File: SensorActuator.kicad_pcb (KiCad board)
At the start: 2 copper layers, 32 parts, among them IC1 STM32L051K8T6, P1 CONN_02X06, P3 CONN_02X04, P4 CONN_01X04, P5 CONN_01X02, Q1 PMosfetGen, Q2 PMosfetGen, Q4 PMosfetGen, Q5 AO3401, SW1 SW_PUSH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

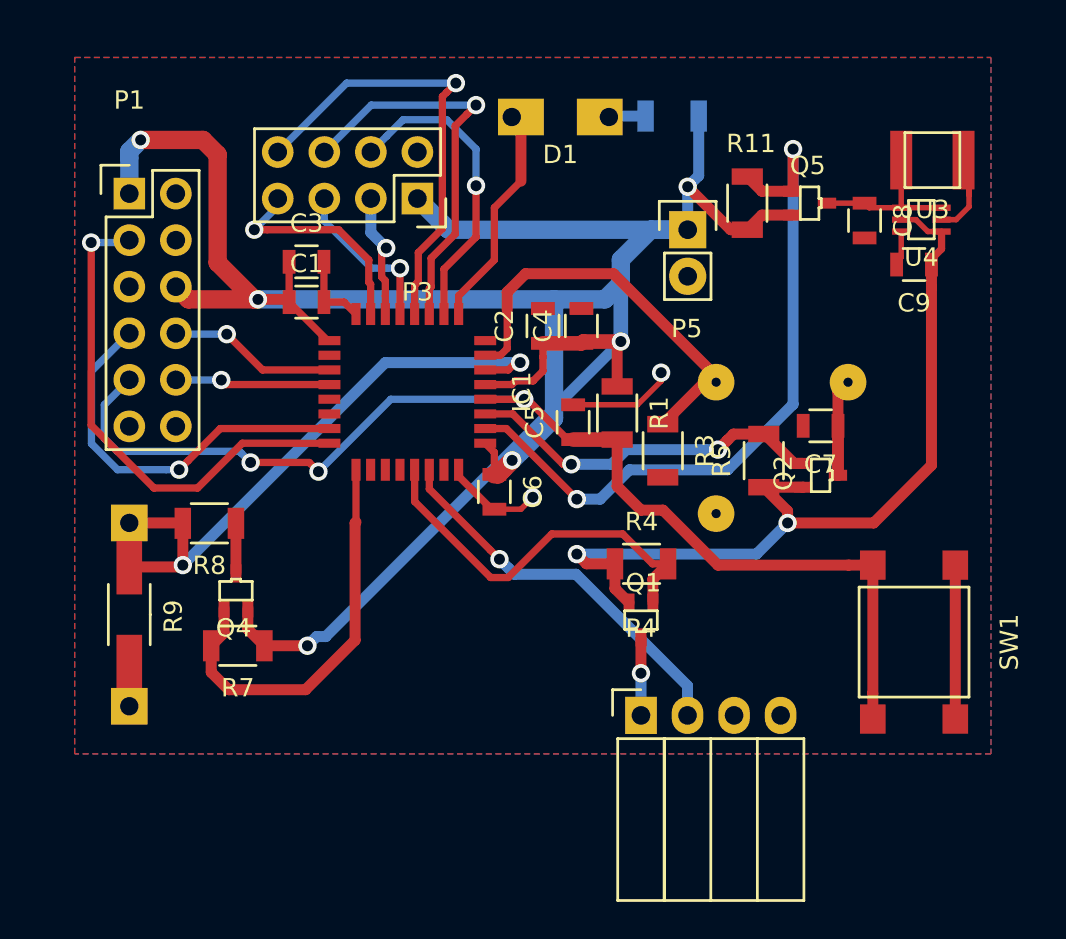
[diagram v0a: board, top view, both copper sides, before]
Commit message: Version 2 of the pcb
 * PCB is now exact 50x38 mm, so we can print it on a small board
 * Through hole components have only a pad on one side,
     this way we are sure we connect the correct pad

Signed-off-by: Philip Luyckx <philip.luyckx@gmail.com>
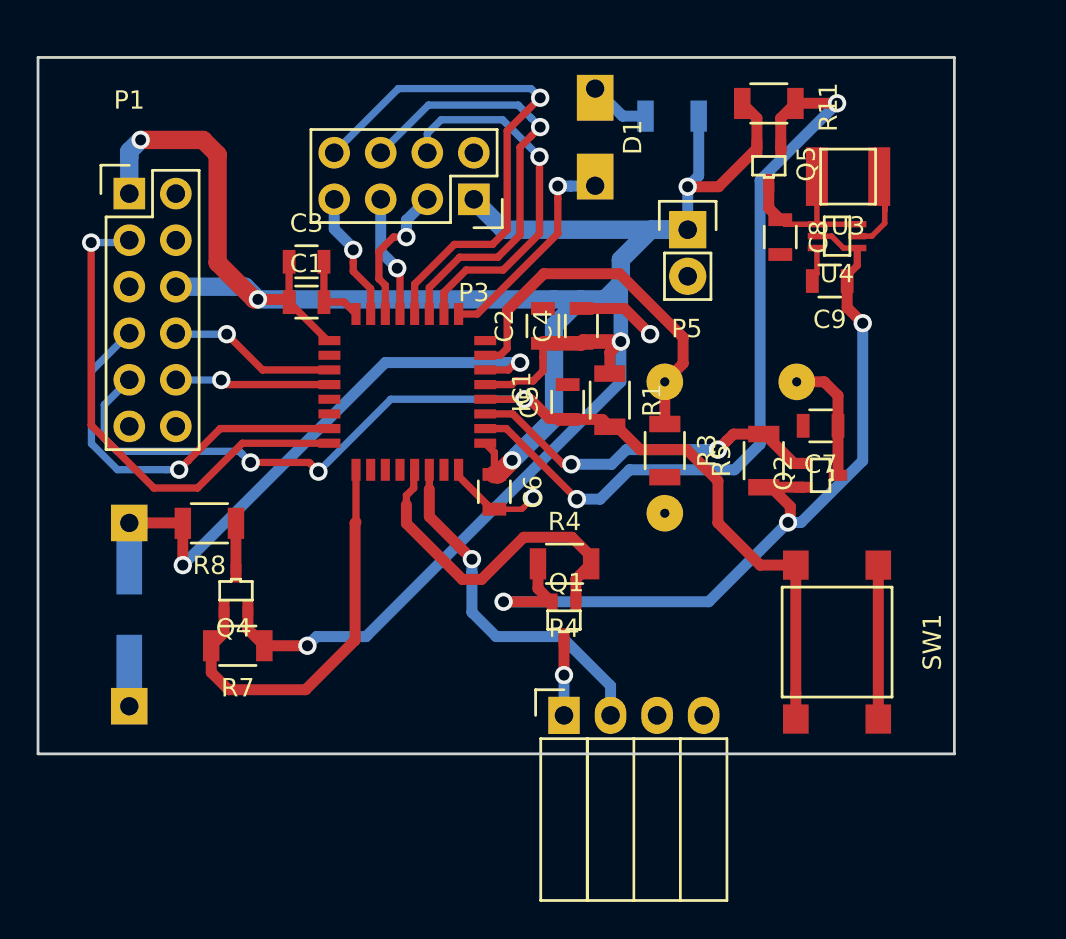
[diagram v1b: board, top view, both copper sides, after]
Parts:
- R9: moved to B.Cu
- moved R11 5.57 mm to (116.9, 59.5), turned to 180 degrees
- moved U4 4.69 mm to (120.6, 66.8)
- moved C9 4.69 mm to (120.2, 69.2)
- moved U3 4.69 mm to (121.2, 63.5)
- moved C8 4.69 mm to (117.5, 66.8)
- moved P4 4.20 mm to (105.7, 92.9)
- moved Q1 4.20 mm to (105.7, 87.7)
- moved R4 4.20 mm to (105.7, 84.6)
- moved SW1 4.20 mm to (120.6, 88.9)
- moved P3 3.08 mm to (100.8, 64.7)
- moved Q5 3.02 mm to (116.9, 62.9), turned to 0 degrees
- moved U1 2.80 mm to (114.8, 78.3)
- moved D1 2.76 mm to (105.8, 61.4), turned to 90 degrees
- moved C5 1.14 mm to (105.9, 75.8)
- moved R1 0.81 mm to (108.2, 75.7)
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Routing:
- net RF_IRQ: track 12.2 -> 7.08 mm
- net MCU_RST: track 63.9 -> 59.7 mm
- net SPI_RF_MISO: track 24.8 -> 28.8 mm
- net Enable5V: track 39.6 -> 43.3 mm
- net RF_CE: track 16.9 -> 20.2 mm
- net SPI_RF_SCK: track 21.8 -> 24.2 mm
- net GND: track 25.7 -> 28.0 mm
- net ADC_Motion: track 22.7 -> 20.4 mm
- net DHT22_Enable: track 21.4 -> 19.1 mm
- net SPI_RF_MOSI: track 9.07 -> 6.99 mm
- net Temp_1Wire: track 21.2 -> 19.6 mm
- net VCC: track 140.2 -> 138.8 mm
- net +5V: track 46.2 -> 47.5 mm, vias 2 -> 3
- net MotionSensor_V+: track 8.01 -> 6.91 mm
- net RF_CSN: track 6.83 -> 7.91 mm
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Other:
- board outline added: 50 x 38 mm

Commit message: Add drill holes
Signed-off-by: Philip Luyckx <philip.luyckx@gmail.com>
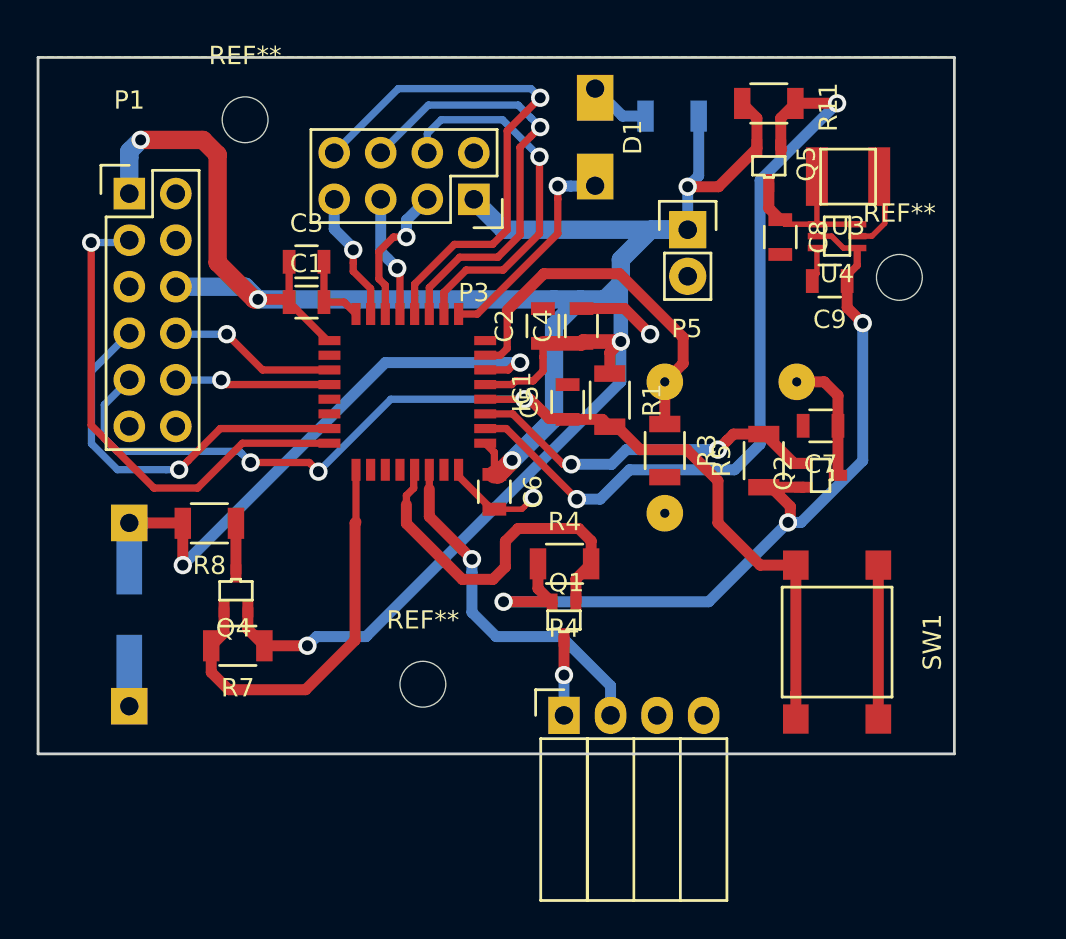
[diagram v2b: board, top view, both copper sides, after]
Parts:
- added REF**: MountingHole_2-5mm, Mounting_Holes:MountingHole_2-5mm, F.Cu at (98.0, 91.2)
- added REF**: MountingHole_2-5mm, Mounting_Holes:MountingHole_2-5mm, F.Cu at (88.3, 60.4)
- added REF**: MountingHole_2-5mm, Mounting_Holes:MountingHole_2-5mm, F.Cu at (124.0, 69.0)
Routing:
- net DHT22_Enable: track 19.1 -> 20.8 mm
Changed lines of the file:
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@@
     (links 86)
     (no_connects 0)
-    (area 76.924999 56.924999 127.075001 95.075001)
+    (area 76.771667 51.15 139.8 103.825001)
     (thickness 1.6)
-    (drawings 6)
-    (tracks 340)
+    (drawings 9)
+    (tracks 342)
     (zones 0)
-    (modules 32)
+    (modules 35)
     (nets 29)
   )
@@
   )
   (setup
-    (last_trace_width 1)
+    (last_trace_width 0.3)
     (user_trace_width 0.3)
     (user_trace_width 0.4)
@@
     )
   )
+  (module Mounting_Holes:MountingHole_2-5mm (layer F.Cu)
+    (at 98 91.2)
+    (descr "Mounting hole, Befestigungsbohrung, 2,5mm, No Annular, Kein Restring,")
+    (tags "Mounting hole, Befestigungsbohrung, 2,5mm, No Annular, Kein Restring,")
+    (fp_text reference REF** (at 0 -3.50012) (layer F.SilkS)
+      (effects (font (size 1 1) (thickness 0.15)))
+    )
+    (fp_text value MountingHole_2-5mm (at 0.09906 3.59918) (layer F.Fab)
+      (effects (font (size 1 1) (thickness 0.15)))
+    )
+    (fp_circle (center 0 0) (end 2.5 0) (layer Cmts.User) (width 0.381))
+    (pad 1 thru_hole circle (at 0 0) (size 2.5 2.5) (drill 2.5) (layers))
+  )
+  (module Mounting_Holes:MountingHole_2-5mm (layer F.Cu)
+    (at 88.3 60.4)
+    (descr "Mounting hole, Befestigungsbohrung, 2,5mm, No Annular, Kein Restring,")
+    (tags "Mounting hole, Befestigungsbohrung, 2,5mm, No Annular, Kein Restring,")
+    (fp_text reference REF** (at 0 -3.50012) (layer F.SilkS)
+      (effects (font (size 1 1) (thickness 0.15)))
+    )
+    (fp_text value MountingHole_2-5mm (at 0.09906 3.59918) (layer F.Fab)
+      (effects (font (size 1 1) (thickness 0.15)))
+    )
+    (fp_circle (center 0 0) (end 2.5 0) (layer Cmts.User) (width 0.381))
+    (pad 1 thru_hole circle (at 0 0) (size 2.5 2.5) (drill 2.5) (layers))
+  )
+  (module Mounting_Holes:MountingHole_2-5mm (layer F.Cu)
+    (at 124 69)
+    (descr "Mounting hole, Befestigungsbohrung, 2,5mm, No Annular, Kein Restring,")
+    (tags "Mounting hole, Befestigungsbohrung, 2,5mm, No Annular, Kein Restring,")
+    (fp_text reference REF** (at 0 -3.50012) (layer F.SilkS)
+      (effects (font (size 1 1) (thickness 0.15)))
+    )
+    (fp_text value MountingHole_2-5mm (at 0.09906 3.59918) (layer F.Fab)
+      (effects (font (size 1 1) (thickness 0.15)))
+    )
+    (fp_circle (center 0 0) (end 2.5 0) (layer Cmts.User) (width 0.381))
+    (pad 1 thru_hole circle (at 0 0) (size 2.5 2.5) (drill 2.5) (layers))
+  )
+  (target plus (at 124 69) (size 2) (width 0.15) (layer Edge.Cuts))
+  (target plus (at 88.3 60.4) (size 2) (width 0.15) (layer Edge.Cuts))
+  (target plus (at 98 91.2) (size 2) (width 0.15) (layer Edge.Cuts))
   (gr_line (start 77 95) (end 77 57) (layer Edge.Cuts) (width 0.15))
   (gr_line (start 127 95) (end 77 95) (layer Edge.Cuts) (width 0.15))
@@
   (segment (start 108.24 92.9) (end 108.24 91.284) (width 0.6) (layer B.Cu) (net 10))
   (segment (start 98.35 79.5) (end 98.35 80.55) (width 0.4) (layer F.Cu) (net 10))
-  (segment (start 103.503666 83.18) (end 106.13 83.18) (width 0.6) (layer F.Cu) (net 11))
-  (segment (start 101.205833 85.477833) (end 103.503666 83.18) (width 0.6) (layer F.Cu) (net 11))
-  (segment (start 106.13 83.18) (end 107.18 84.23) (width 0.6) (layer F.Cu) (net 11))
-  (segment (start 100.149829 85.477833) (end 101.205833 85.477833) (width 0.6) (layer F.Cu) (net 11))
-  (segment (start 107.18 84.23) (end 107.18 84.63) (width 0.6) (layer F.Cu) (net 11))
   (segment (start 97.1 81.4) (end 97.1 82.428004) (width 0.6) (layer F.Cu) (net 11))
   (segment (start 97.1 82.428004) (end 100.149829 85.477833) (width 0.6) (layer F.Cu) (net 11))
+  (segment (start 102.5 84.8) (end 102.5 83.4) (width 0.6) (layer F.Cu) (net 11))
+  (segment (start 100.149829 85.477833) (end 101.822167 85.477833) (width 0.6) (layer F.Cu) (net 11))
+  (segment (start 102.5 83.4) (end 103.2 82.7) (width 0.6) (layer F.Cu) (net 11))
+  (segment (start 101.822167 85.477833) (end 102.5 84.8) (width 0.6) (layer F.Cu) (net 11))
+  (segment (start 103.2 82.7) (end 106.5 82.7) (width 0.6) (layer F.Cu) (net 11))
+  (segment (start 106.5 82.7) (end 107.18 83.38) (width 0.6) (layer F.Cu) (net 11))
+  (segment (start 107.18 83.38) (end 107.18 84.63) (width 0.6) (layer F.Cu) (net 11))
   (segment (start 97.55 79.5) (end 97.500001 79.549999) (width 0.4) (layer F.Cu) (net 11))
   (segment (start 97.500001 79.549999) (end 97.500001 80.500001) (width 0.4) (layer F.Cu) (net 11))
@@
     )
   )
-  (zone (net 3) (net_name GND) (layer F.Cu) (hatch edge 0.508)
-    (connect_pads (clearance 0.2))
-    (min_thickness 0.254)
-    (fill yes (arc_segments 16) (thermal_gap 0.508) (thermal_bridge_width 0.508))
-    (polygon
-      (pts
-        (xy 77 57) (xy 127 57) (xy 127 95) (xy 77 95)
-      )
-    )
-  )
   (zone (net 0) (net_name "") (layer F.Cu) (hatch edge 0.508)
     (connect_pads (clearance 0.2))
@@
       )
     )
+  )
+  (zone (net 3) (net_name GND) (layer F.Cu) (hatch edge 0.508)
+    (connect_pads (clearance 0.2))
+    (min_thickness 0.254)
+    (fill yes (arc_segments 16) (thermal_gap 0.508) (thermal_bridge_width 0.508))
+    (polygon
+      (pts
+        (xy 77 57) (xy 127 57) (xy 127 95) (xy 77 95)
+      )
+    )

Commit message: Remove VCC from UART-DBG connector
 * VCC of a USB-TTL connector may not be connected to VCC of the board.
     The usb will put 3.3V (or 5V) on this pin, so we will create a short
     circuit if we connect the TLL and use a battery as supply.

Signed-off-by: Philip Luyckx <philip.luyckx@gmail.com>
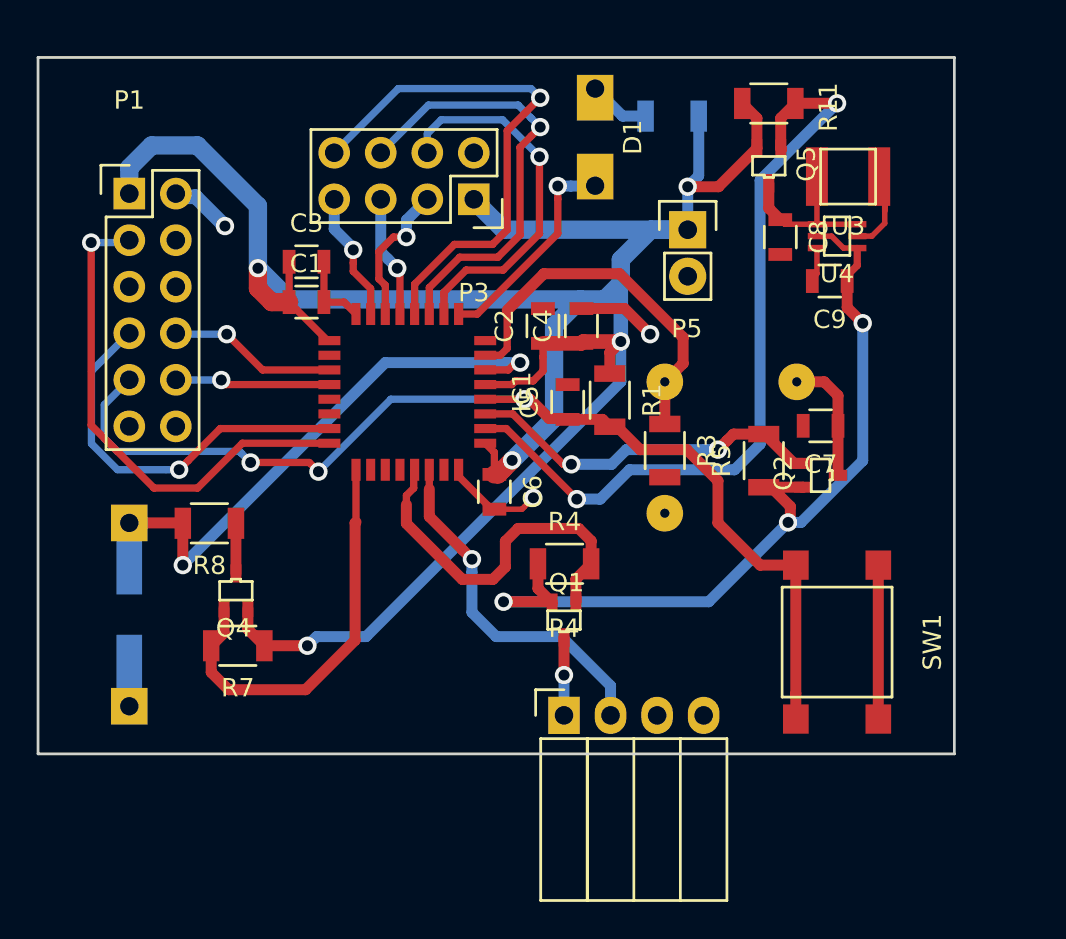
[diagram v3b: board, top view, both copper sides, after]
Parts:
- removed REF** (x3): MountingHole_2-5mm, Mounting_Holes:MountingHole_2-5mm
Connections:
- C1 pad 1: VCC -> +BATT
- C2 pad 1: VCC -> +BATT
- C3 pad 1: VCC -> +BATT
- C4 pad 1: VCC -> +BATT
- C6 pad 1: VCC -> +BATT
- IC1 pad 1: VCC -> +BATT
- IC1 pad 17: VCC -> +BATT
- IC1 pad 18: (no net) -> Net-(IC1-Pad18)
- IC1 pad 21: (no net) -> Net-(IC1-Pad21)
- IC1 pad 22: (no net) -> Net-(IC1-Pad22)
- IC1 pad 26: (no net) -> Net-(IC1-Pad26)
- IC1 pad 27: (no net) -> Net-(IC1-Pad27)
- IC1 pad 28: (no net) -> Net-(IC1-Pad28)
- IC1 pad 31: (no net) -> Net-(IC1-Pad31)
- IC1 pad 5: VCC -> +BATT
- IC1 pad 8: (no net) -> Net-(IC1-Pad8)
- P1 pad 1: VCC -> +BATT
- P1 pad 11: (no net) -> Net-(P1-Pad11)
- P1 pad 12: (no net) -> Net-(P1-Pad12)
- P1 pad 4: (no net) -> Net-(P1-Pad4)
- P1 pad 6: VCC -> Net-(P1-Pad6)
- P3 pad 1: VCC -> +BATT
- P5 pad 1: VCC -> +BATT
- Q4 pad 2: VCC -> +BATT
- Q5 pad 2: VCC -> +BATT
- R1 pad 1: VCC -> +BATT
- R11 pad 2: VCC -> +BATT
- R2 pad 1: VCC -> +BATT
- R7 pad 1: VCC -> +BATT
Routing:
- net VCC: track 138.8 -> 0.00 mm, vias 6 -> 0
- net +BATT: track 0.00 -> 133.4 mm, vias 0 -> 5
- net GND: track 28.0 -> 31.4 mm, vias 2 -> 3

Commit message: Increase clearance for fill zones to 0.4mm
Signed-off-by: Philip Luyckx <philip.luyckx@gmail.com>
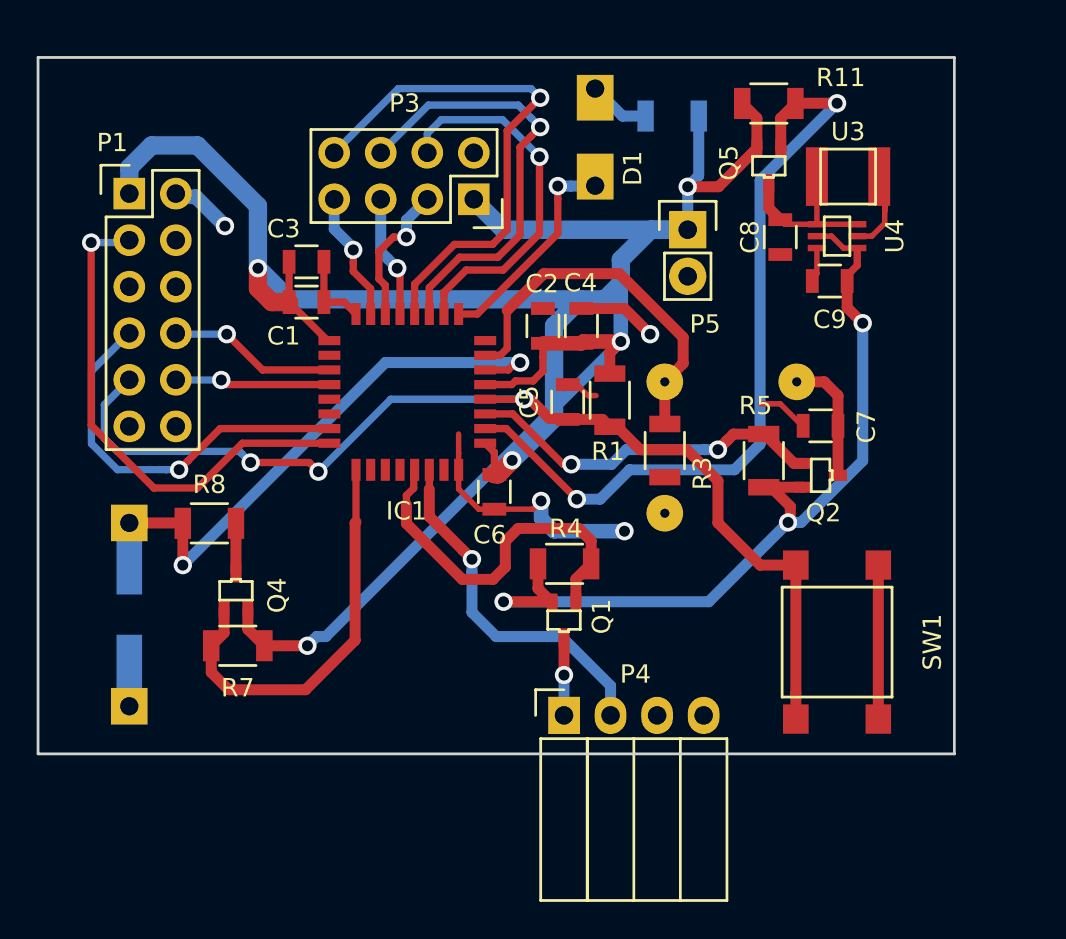
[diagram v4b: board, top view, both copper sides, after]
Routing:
- net GND: track 31.4 -> 45.0 mm, vias 3 -> 4
- net +BATT: track 133.4 -> 132.1 mm
